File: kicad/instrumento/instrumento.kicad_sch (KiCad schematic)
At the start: 2 parts, among them U1 Teensy4.1, U2 Teensy4.0_AudioShield_REVD

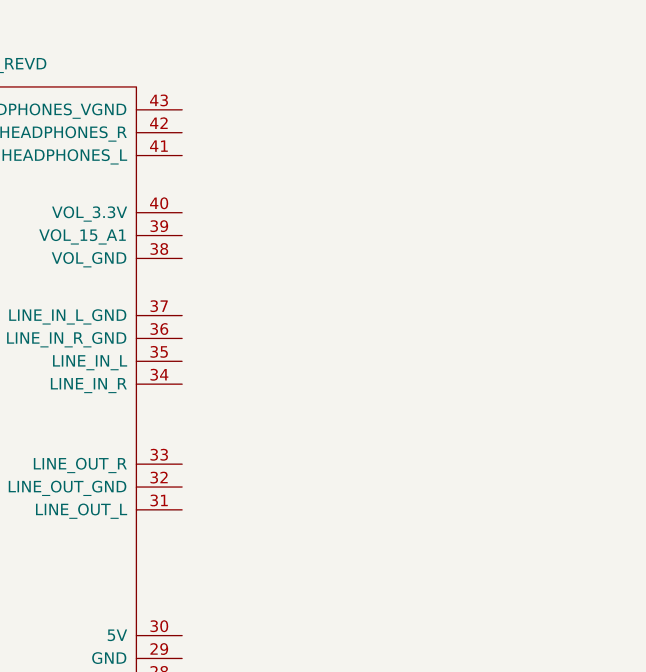
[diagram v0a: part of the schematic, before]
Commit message: Add DRV134
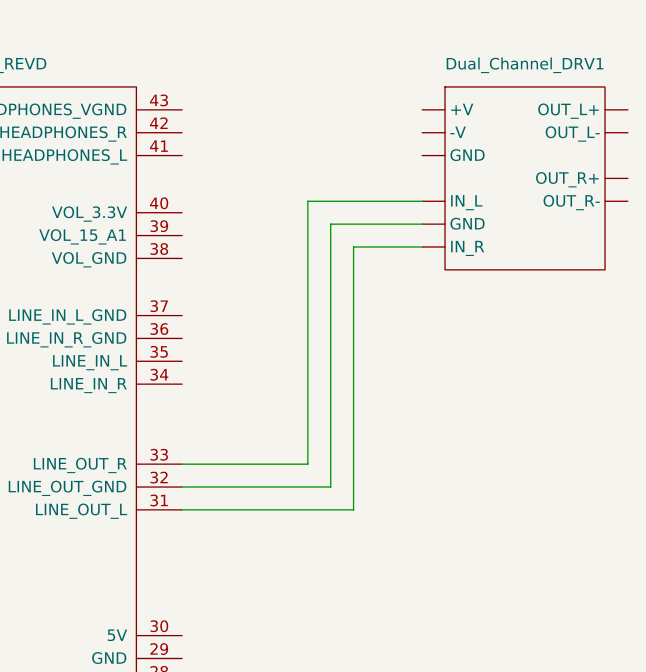
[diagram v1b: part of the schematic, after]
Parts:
- added Dual_Channel_DRV1: (no value), symbol parts:Dual_Channel_DRV134
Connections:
- net at U2.31 (LINE_OUT_L): now also Dual_Channel_DRV1. (OUT_R-)
- net at U2.32 (LINE_OUT_GND): now also Dual_Channel_DRV1. (OUT_R-)
- net at U2.33 (LINE_OUT_R): now also Dual_Channel_DRV1. (OUT_R-)
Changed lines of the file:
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@@
 	(generator_version "10.0")
 	(paper "A4")
+	(wire
+		(pts
+			(xy 162.56 81.28) (xy 179.07 81.28)
+		)
+		(stroke
+			(width 0)
+			(type default)
+		)
+	)
+	(wire
+		(pts
+			(xy 179.07 81.28) (xy 179.07 52.07)
+		)
+		(stroke
+			(width 0)
+			(type default)
+		)
+	)
+	(wire
+		(pts
+			(xy 162.56 83.82) (xy 181.61 83.82)
+		)
+		(stroke
+			(width 0)
+			(type default)
+		)
+	)
+	(wire
+		(pts
+			(xy 162.56 78.74) (xy 176.53 78.74)
+		)
+		(stroke
+			(width 0)
+			(type default)
+		)
+	)
+	(wire
+		(pts
+			(xy 181.61 54.61) (xy 189.23 54.61)
+		)
+		(stroke
+			(width 0)
+			(type default)
+		)
+	)
+	(wire
+		(pts
+			(xy 181.61 83.82) (xy 181.61 54.61)
+		)
+		(stroke
+			(width 0)
+			(type default)
+		)
+	)
+	(wire
+		(pts
+			(xy 176.53 78.74) (xy 176.53 49.53)
+		)
+		(stroke
+			(width 0)
+			(type default)
+		)
+	)
+	(wire
+		(pts
+			(xy 176.53 49.53) (xy 189.23 49.53)
+		)
+		(stroke
+			(width 0)
+			(type default)
+		)
+	)
+	(wire
+		(pts
+			(xy 179.07 52.07) (xy 189.23 52.07)
+		)
+		(stroke
+			(width 0)
+			(type default)
+		)
+	)
 	(symbol
 		(lib_id "teensy:Teensy4.1")
@@
 					(unit 1)
 				)
+			)
+		)
+	)
+	(symbol
+		(lib_id "parts:Dual_Channel_DRV134")
+		(at 191.77 54.61 0)
+		(unit 1)
+		(body_style 1)
+		(exclude_from_sim no)
+		(in_bom yes)
+		(on_board yes)
+		(in_pos_files yes)
+		(dnp no)
+		(fields_autoplaced yes)
+		(property "Reference" "Dual_Channel_DRV1"
+			(at 200.66 34.29 0)
+			(show_name no)
+			(do_not_autoplace no)
+			(effects
+				(font
+					(size 1.27 1.27)
+				)
+			)
+		)
+		(property "Value" ""
+			(at 191.77 54.61 0)
+			(show_name no)
+			(do_not_autoplace no)
+			(effects
+				(font
+					(size 1.27 1.27)
+				)
+			)
+		)
+		(property "Footprint" ""
+			(at 191.77 54.61 0)
+			(hide yes)
+			(show_name no)
+			(do_not_autoplace no)
+			(effects
+				(font
+					(size 1.27 1.27)
+				)
+			)
+		)
+		(property "Datasheet" ""
+			(at 191.77 54.61 0)
+			(hide yes)
+			(show_name no)
+			(do_not_autoplace no)
+			(effects
+				(font
+					(size 1.27 1.27)
+				)
+			)
+		)
+		(property "Description" ""
+			(at 191.77 54.61 0)
+			(hide yes)
+			(show_name no)
+			(do_not_autoplace no)
+			(effects
+				(font
+					(size 1.27 1.27)
+				)
+			)
+		)
+		(pin ""
+		)
+		(pin ""
+		)
+		(pin ""
+		)
+		(pin ""
+		)
+		(pin ""
+		)
+		(pin ""
+		)
+		(pin ""
+		)
+		(pin ""
+		)
+		(pin ""
+		)
+		(pin ""
+		)
+		(instances
+			(project "instrumento"
+				(path "/7badb4e4-eed3-457a-a043-e5ce7a94b62c"
+					(reference "Dual_Channel_DRV1")
+					(unit 1)
+				)

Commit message: Add power
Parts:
- added B1: (no value), symbol parts:20_Symmetric_Boost
- renumbered Dual_Channel_DRV1 to D1
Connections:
- net at U2.31 (LINE_OUT_L): no longer D1. (OUT_R-)
- net at U2.32 (LINE_OUT_GND): no longer D1. (OUT_R-)
- net at U2.33 (LINE_OUT_R): no longer D1. (OUT_R-)
- new net: B1. (GND), D1. (OUT_R-) (x3)
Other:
- moved on the sheet: D1, U1, U2
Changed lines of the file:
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@@
 	(generator_version "10.0")
 	(paper "A4")
-	(wire
-		(pts
-			(xy 162.56 81.28) (xy 179.07 81.28)
-		)
-		(stroke
-			(width 0)
-			(type default)
-		)
-	)
-	(wire
-		(pts
-			(xy 179.07 81.28) (xy 179.07 52.07)
-		)
-		(stroke
-			(width 0)
-			(type default)
-		)
-	)
-	(wire
-		(pts
-			(xy 162.56 83.82) (xy 181.61 83.82)
-		)
-		(stroke
-			(width 0)
-			(type default)
-		)
-	)
-	(wire
-		(pts
-			(xy 162.56 78.74) (xy 176.53 78.74)
-		)
-		(stroke
-			(width 0)
-			(type default)
-		)
-	)
-	(wire
-		(pts
-			(xy 181.61 54.61) (xy 189.23 54.61)
-		)
-		(stroke
-			(width 0)
-			(type default)
-		)
-	)
-	(wire
-		(pts
-			(xy 181.61 83.82) (xy 181.61 54.61)
-		)
-		(stroke
-			(width 0)
-			(type default)
-		)
-	)
-	(wire
-		(pts
-			(xy 176.53 78.74) (xy 176.53 49.53)
-		)
-		(stroke
-			(width 0)
-			(type default)
-		)
-	)
-	(wire
-		(pts
-			(xy 176.53 49.53) (xy 189.23 49.53)
-		)
-		(stroke
-			(width 0)
-			(type default)
-		)
-	)
-	(wire
-		(pts
-			(xy 179.07 52.07) (xy 189.23 52.07)
+	(junction
+		(at 209.55 26.67)
+		(diameter 0)
+		(color 0 0 0 0)
+	)
+	(wire
+		(pts
+			(xy 209.55 26.67) (xy 210.82 26.67)
+		)
+		(stroke
+			(width 0)
+			(type default)
+		)
+	)
+	(wire
+		(pts
+			(xy 207.01 53.34) (xy 219.71 53.34)
+		)
+		(stroke
+			(width 0)
+			(type default)
+		)
+	)
+	(wire
+		(pts
+			(xy 209.55 50.8) (xy 219.71 50.8)
+		)
+		(stroke
+			(width 0)
+			(type default)
+		)
+	)
+	(wire
+		(pts
+			(xy 212.09 24.13) (xy 207.01 24.13)
+		)
+		(stroke
+			(width 0)
+			(type default)
+		)
+	)
+	(wire
+		(pts
+			(xy 212.09 48.26) (xy 212.09 24.13)
+		)
+		(stroke
+			(width 0)
+			(type default)
+		)
+	)
+	(wire
+		(pts
+			(xy 209.55 26.67) (xy 209.55 50.8)
+		)
+		(stroke
+			(width 0)
+			(type default)
+		)
+	)
+	(wire
+		(pts
+			(xy 207.01 31.75) (xy 207.01 53.34)
+		)
+		(stroke
+			(width 0)
+			(type default)
+		)
+	)
+	(wire
+		(pts
+			(xy 207.01 26.67) (xy 209.55 26.67)
+		)
+		(stroke
+			(width 0)
+			(type default)
+		)
+	)
+	(wire
+		(pts
+			(xy 219.71 48.26) (xy 212.09 48.26)
 		)
 		(stroke
@@
 	(symbol
 		(lib_id "teensy:Teensy4.1")
-		(at 59.69 96.52 0)
+		(at 54.61 119.38 0)
 		(unit 1)
 		(body_style 1)
@@
 		(fields_autoplaced yes)
 		(property "Reference" "U1"
-			(at 59.69 30.48 0)
+			(at 54.61 53.34 0)
 			(show_name no)
 			(do_not_autoplace no)
@@
 		)
 		(property "Value" "Teensy4.1"
-			(at 59.69 33.02 0)
+			(at 54.61 55.88 0)
 			(show_name no)
 			(do_not_autoplace no)
@@
 		)
 		(property "Footprint" ""
-			(at 49.53 86.36 0)
+			(at 44.45 109.22 0)
 			(hide yes)
 			(show_name no)
@@
 		)
 		(property "Datasheet" ""
-			(at 49.53 86.36 0)
+			(at 44.45 109.22 0)
 			(hide yes)
 			(show_name no)
@@
 		)
 		(property "Description" ""
-			(at 59.69 96.52 0)
+			(at 54.61 119.38 0)
 			(hide yes)
 			(show_name no)
@@
 	)
 	(symbol
-		(lib_id "parts:Dual_Channel_DRV134")
-		(at 191.77 54.61 0)
+		(lib_id "parts:20_Symmetric_Boost")
+		(at 194.31 24.13 0)
 		(unit 1)
 		(body_style 1)
@@
 		(dnp no)
 		(fields_autoplaced yes)
-		(property "Reference" "Dual_Channel_DRV1"
-			(at 200.66 34.29 0)
+		(property "Reference" "B1"
+			(at 199.39 19.05 0)
 			(show_name no)
 			(do_not_autoplace no)
@@
 		)
 		(property "Value" ""
-			(at 191.77 54.61 0)
+			(at 194.31 24.13 0)
 			(show_name no)
 			(do_not_autoplace no)
@@
 		)
 		(property "Footprint" ""
-			(at 191.77 54.61 0)
+			(at 194.31 24.13 0)
 			(hide yes)
 			(show_name no)
@@
 		)
 		(property "Datasheet" ""
-			(at 191.77 54.61 0)
+			(at 194.31 24.13 0)
 			(hide yes)
 			(show_name no)
@@
 		)
 		(property "Description" ""
-			(at 191.77 54.61 0)
-			(hide yes)
-			(show_name no)
-			(do_not_autoplace no)
-			(effects
-				(font
-					(size 1.27 1.27)
-				)
-			)
-		)
-		(pin ""
-		)
-		(pin ""
-		)
-		(pin ""
-		)
-		(pin ""
-		)
-		(pin ""
+			(at 194.31 24.13 0)
+			(hide yes)
+			(show_name no)
+			(do_not_autoplace no)
+			(effects
+				(font
+					(size 1.27 1.27)
+				)
+			)
 		)
 		(pin ""
@@
 			(project "instrumento"
 				(path "/7badb4e4-eed3-457a-a043-e5ce7a94b62c"
-					(reference "Dual_Channel_DRV1")
+					(reference "B1")
+					(unit 1)
+				)
+			)
+		)
+	)
+	(symbol
+		(lib_id "parts:Dual_Channel_DRV134")
+		(at 222.25 63.5 0)
+		(unit 1)
+		(body_style 1)
+		(exclude_from_sim no)
+		(in_bom yes)
+		(on_board yes)
+		(in_pos_files yes)
+		(dnp no)
+		(fields_autoplaced yes)
+		(property "Reference" "D1"
+			(at 231.14 43.18 0)
+			(show_name no)
+			(do_not_autoplace no)
+			(effects
+				(font
+					(size 1.27 1.27)
+				)
+			)
+		)
+		(property "Value" ""
+			(at 222.25 63.5 0)
+			(show_name no)
+			(do_not_autoplace no)
+			(effects
+				(font
+					(size 1.27 1.27)
+				)
+			)
+		)
+		(property "Footprint" ""
+			(at 222.25 63.5 0)
+			(hide yes)
+			(show_name no)
+			(do_not_autoplace no)
+			(effects
+				(font
+					(size 1.27 1.27)
+				)
+			)
+		)
+		(property "Datasheet" ""
+			(at 222.25 63.5 0)
+			(hide yes)
+			(show_name no)
+			(do_not_autoplace no)
+			(effects
+				(font
+					(size 1.27 1.27)
+				)
+			)
+		)
+		(property "Description" ""
+			(at 222.25 63.5 0)
+			(hide yes)
+			(show_name no)
+			(do_not_autoplace no)
+			(effects
+				(font
+					(size 1.27 1.27)
+				)
+			)
+		)
+		(pin ""
+		)
+		(pin ""
+		)
+		(pin ""
+		)
+		(pin ""
+		)
+		(pin ""
+		)
+		(pin ""
+		)
+		(pin ""
+		)
+		(pin ""
+		)
+		(pin ""
+		)
+		(pin ""
+		)
+		(instances
+			(project "instrumento"
+				(path "/7badb4e4-eed3-457a-a043-e5ce7a94b62c"
+					(reference "D1")
 					(unit 1)
 				)
@@
 	(symbol
 		(lib_id "teensy_audio_shield:Teensy4.0_AudioShield_REVD")
-		(at 134.62 73.66 0)
+		(at 137.16 110.49 0)
 		(unit 1)
 		(body_style 1)
@@
 		(fields_autoplaced yes)
 		(property "Reference" "U2"
-			(at 134.62 31.75 0)
+			(at 137.16 68.58 0)
 			(show_name no)
 			(do_not_autoplace no)
@@
 		)
 		(property "Value" "Teensy4.0_AudioShield_REVD"
-			(at 134.62 34.29 0)
+			(at 137.16 71.12 0)
 			(show_name no)
 			(do_not_autoplace no)
@@
 		)
 		(property "Footprint" ""
-			(at 124.46 68.58 0)
+			(at 127 105.41 0)
 			(hide yes)
 			(show_name no)
@@
 		)
 		(property "Datasheet" ""
-			(at 124.46 68.58 0)
+			(at 127 105.41 0)
 			(hide yes)
 			(show_name no)
@@
 		)
 		(property "Description" ""
-			(at 134.62 73.66 0)
-			(hide yes)
-			(show_name no)
+			(at 137.16 110.49 0)
+			(hide yes)
+			(show_name no)

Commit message: Audio output
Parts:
- removed B1: (no value), symbol parts:20_Symmetric_Boost
- added J1: Left, symbol Connector_Audio:AudioJack3_SwitchTR
- added J2: Right, symbol Connector_Audio:AudioJack3_SwitchTR
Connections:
- net GND: now reaches U1.1 (GND)
- net GND: now also D1. (OUT_R-), U2.29 (GND), J1.S, J2.S
- net +5V: now reaches U1.48 (VIN)
- net +5V: now also U2.30 (5V)
- net at U2.31 (LINE_OUT_L): now also D1. (OUT_R-)
- net at U2.32 (LINE_OUT_GND): now also D1. (OUT_R-)
- net at U2.33 (LINE_OUT_R): now also D1. (OUT_R-)
- new net: D1. (OUT_R-), J2.R
- new net: D1. (OUT_R-), J2.T
- new net: D1. (OUT_R-), J1.R
- new net: D1. (OUT_R-), J1.T
- new net +15V: D1. (OUT_R-)
- new net -15V: D1. (OUT_R-)
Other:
- moved on the sheet: D1, U1, U2
